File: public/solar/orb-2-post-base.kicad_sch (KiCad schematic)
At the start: 17 parts, among them U1 LMR16030, U2 74AHCT125

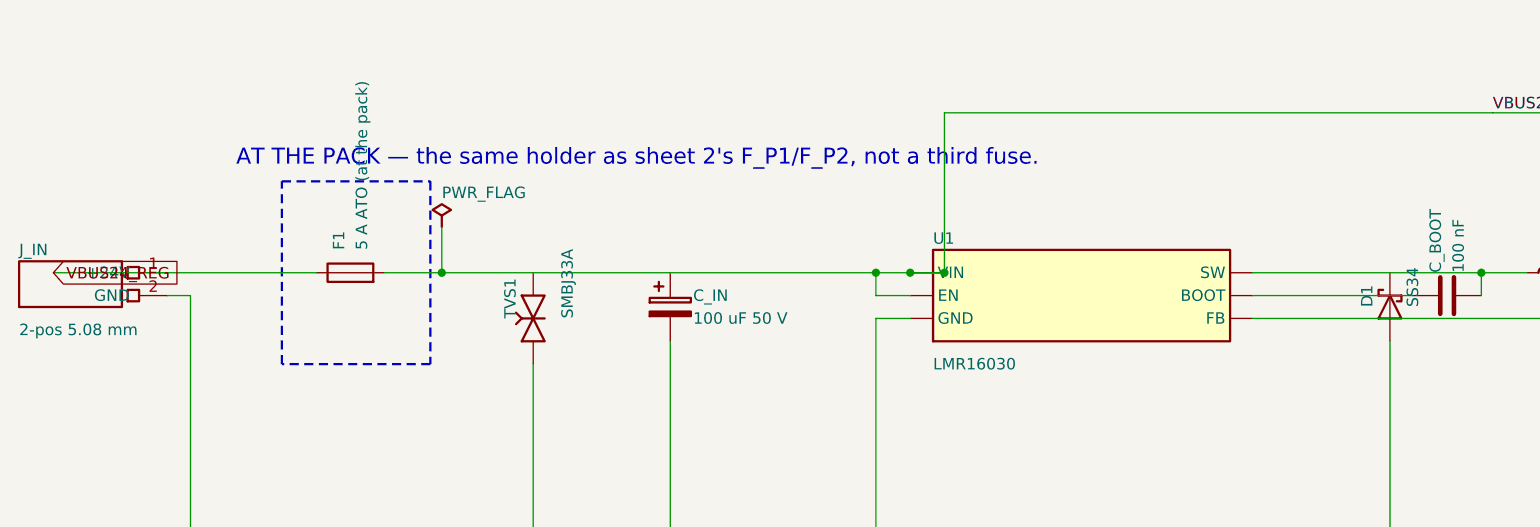
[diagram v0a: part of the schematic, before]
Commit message: solar: fab section, animation fixes, tunable copy, F1 gone
Co-Authored-By: Claude Fable 5 <noreply@anthropic.com>
Claude-Session: https://claude.ai/code/session_01KGs7HAmqeyDzRmkLXBVjfP
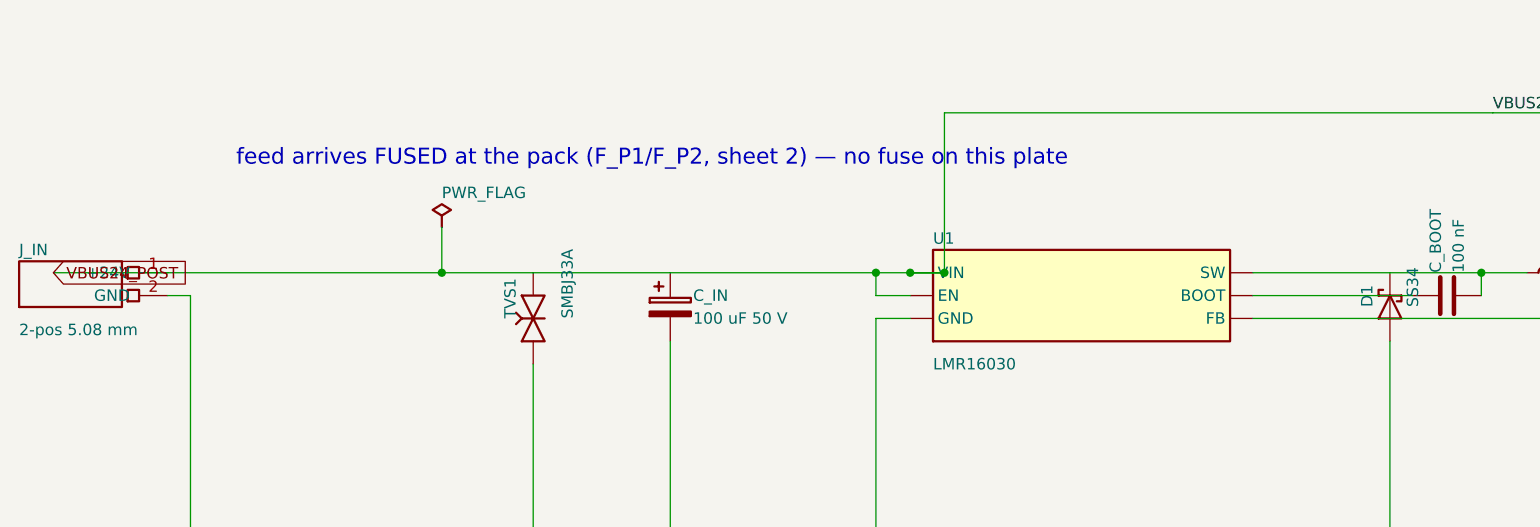
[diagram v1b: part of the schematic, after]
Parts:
- removed F1: 5 A ATO (at the pack), symbol moistlab:Fuse
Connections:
- net VBUS24_REG is gone; now on net VBUS24_POST: J_IN.1 (+24V)
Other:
- note added: "feed arrives FUSED at the pack (F_P1/F_P2, sheet 2) — no fuse on this plate"
- note removed: "AT THE PACK — the same holder as sheet 2's F_P1/F_P2, not a third fuse."
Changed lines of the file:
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@@
 		(comment 1 "one per post — modules on a plate, no custom PCB")
 	)
-	(rectangle (start 43.18 63.5) (end 59.69 83.82) (stroke (width 0.254) (type dash)) (fill (type none)))
 	(wire (pts (xy 17.78 73.66) (xy 30.48 73.66)) (stroke (width 0) (type default)))
-	(wire (pts (xy 30.48 73.66) (xy 46.99 73.66)) (stroke (width 0) (type default)))
-	(wire (pts (xy 54.61 73.66) (xy 60.96 73.66)) (stroke (width 0) (type default)))
+	(wire (pts (xy 30.48 73.66) (xy 60.96 73.66)) (stroke (width 0) (type default)))
 	(wire (pts (xy 60.96 73.66) (xy 71.12 73.66)) (stroke (width 0) (type default)))
 	(wire (pts (xy 71.12 73.66) (xy 86.36 73.66)) (stroke (width 0) (type default)))
@@
 	(junction (at 226.06 152.4) (diameter 0) (color 0 0 0 0))
 	(no_connect (at 247.65 200.66))
-	(global_label "VBUS24_REG" (at 17.78 73.66 0) (shape input) (effects (font (size 1.27 1.27)) (justify left)))
+	(global_label "VBUS24_POST" (at 17.78 73.66 0) (shape input) (effects (font (size 1.27 1.27)) (justify left)))
 	(label "GND" (at 114.3 152.4 0) (effects (font (size 1.27 1.27)) (justify left bottom)))
 	(label "+5V_BASE" (at 193.04 73.66 0) (effects (font (size 1.27 1.27)) (justify left bottom)))
@@
 	(label "SCL" (at 294.64 185.42 0) (effects (font (size 1.27 1.27)) (justify left bottom)))
 	(label "VBUS24_POST" (at 177.8 55.88 0) (effects (font (size 1.27 1.27)) (justify left bottom)))
-	(text "AT THE PACK — the same holder as sheet 2's F_P1/F_P2, not a third fuse." (exclude_from_sim no) (at 38.1 60.96 0) (effects (font (size 1.778 1.778)) (justify left)))
+	(text "feed arrives FUSED at the pack (F_P1/F_P2, sheet 2) — no fuse on this plate" (exclude_from_sim no) (at 38.1 60.96 0) (effects (font (size 1.778 1.778)) (justify left)))
 	(text "4th buffer spare: input to ground, output-enable HIGH so it is disabled, output not connected." (exclude_from_sim no) (at 248.92 226.06 0) (effects (font (size 1.651 1.651)) (justify left)))
 	(text "I2C up the riser to the sensors in the globes." (exclude_from_sim no) (at 271.78 190.5 0) (effects (font (size 1.651 1.651)) (justify left)))
@@
 		(instances (project "orb" (path "/75a76274-4a9c-536f-ada1-808fa82cab8d" (reference "J_IN") (unit 1))))
 	)
-	(symbol (lib_id "moistlab:Fuse") (at 50.8 73.66 90) (unit 1)
-		(exclude_from_sim no) (in_bom yes) (on_board yes) (dnp no)
-		(property "Reference" "F1" (at 49.53 71.12 0) (effects (font (size 1.27 1.27)) (justify left)))
-		(property "Value" "5 A ATO (at the pack)" (at 52.07 71.12 0) (effects (font (size 1.27 1.27)) (justify left)))
-		(property "Footprint" "" (at 50.8 73.66 0) (effects (font (size 1.27 1.27)) (hide yes)))
-		(pin "1")
-		(pin "2")
-		(instances (project "orb" (path "/75a76274-4a9c-536f-ada1-808fa82cab8d" (reference "F1") (unit 1))))
-	)
 	(symbol (lib_id "moistlab:D_TVS") (at 71.12 78.74 90) (unit 1)
